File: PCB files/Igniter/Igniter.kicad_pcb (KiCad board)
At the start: 2 copper layers, 124.9 x 69.6 mm, 57 parts, among them IC1 74HC4050, J1 PT, J10 SL2, J11 SL3, J12 SL4, J13 SL5, J14 Micro_SD_Card, J2 PT, J3 PT, J4 PT, J5 Battery +, J6 Battery -, J7 Ignition Coil +, J8 Ignition coil -, J9 SL1, Q1 N MOSFET, Q2 N MOSFET, Q3 N MOSFET, Q4 N MOSFET, Q5 N MOSFET, Q6 N MOSFET, SW1 ARM, U2 FDS8984, U3 FDS8984, U4 FDS8984

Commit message: 12/10/2019
PCB
-Increased 24V trace width to 1 mm
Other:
- net class 24V: trace_width 0.4 -> 1
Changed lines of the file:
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@@
   (net_class 24V ""
     (clearance 0.2)
-    (trace_width 0.4)
+    (trace_width 1)
     (via_dia 0.8)
     (via_drill 0.4)

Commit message: 12/10/2019
-Selected battery molex connector footprint
-Read netlist
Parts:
- removed the J6 at (226.3, 109.0)
- D12: value 3V3 -> 3V3_GOOD
- D13: value 24V -> 24V_ARMED
- J5: value Battery + -> Battery; footprint IgniterCustom:BananaJack15.5mm -> Connector_Molex:Molex_Mini-Fit_Jr_5566-02A_2x01_P4.20mm_Vertical
- moved J5 33.0 mm to (195.6, 105.0), turned to 90 degrees
- moved J10 0.46 mm to (117.1, 143.9)
- moved J11 0.46 mm to (125.4, 143.9)
- moved J12 0.46 mm to (133.6, 143.9)
- moved J8 0.46 mm to (100.7, 143.9)
- moved J9 0.46 mm to (108.9, 143.9)
- renumbered J11 to J10, J12 to J11, J13 to J12, J14 to J13, J7 to J6, J8 to J7, J9 to J8, J10 to J9
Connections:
- J5 pad 2: (no net) -> GNDREF

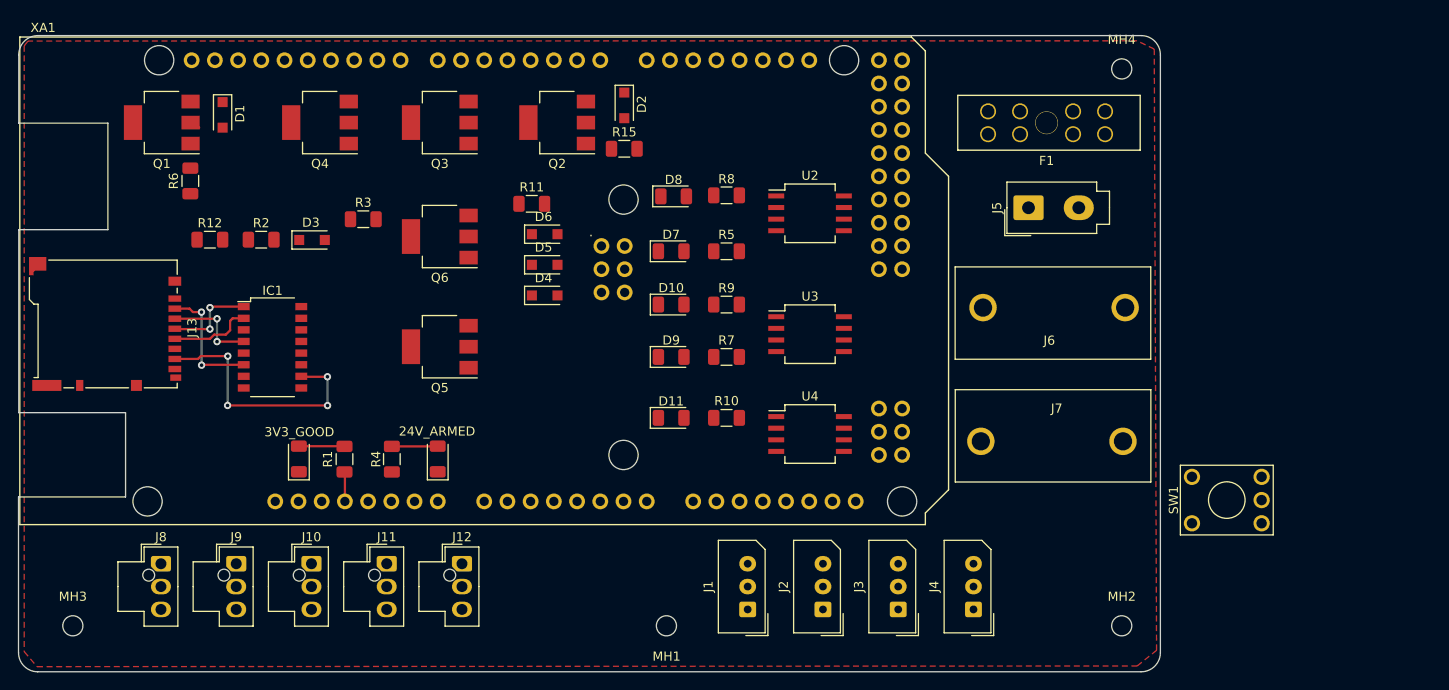
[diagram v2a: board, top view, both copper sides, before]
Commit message: 12/17/2019
-Board layout changes to make better routing paths, no traces drawn yet
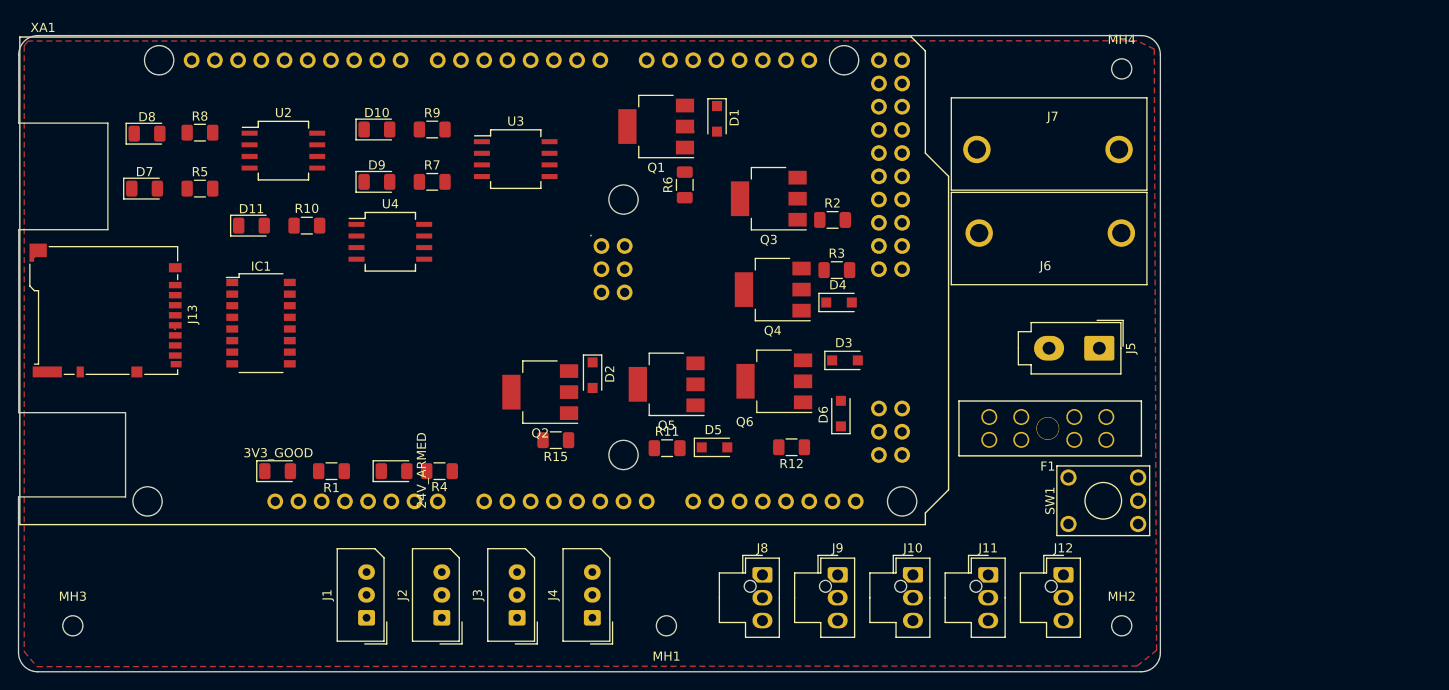
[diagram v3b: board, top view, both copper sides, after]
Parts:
- moved R12 67.6 mm to (169.7, 131.2), turned to 180 degrees
- moved J11 65.8 mm to (191.2, 145.1)
- moved J10 65.8 mm to (182.9, 145.1)
- moved J12 65.8 mm to (199.4, 145.1)
- moved J8 65.8 mm to (166.5, 145.1)
- moved J9 65.8 mm to (174.7, 145.1)
- moved R2 62.5 mm to (174.1, 106.3)
- moved D3 59.8 mm to (175.5, 121.7)
- moved D8 58.0 mm to (99.1, 96.9)
- moved R8 58.0 mm to (104.9, 96.7)
- moved U2 58.0 mm to (114.1, 98.7)
- moved D7 58.0 mm to (98.9, 102.9)
- moved R5 58.0 mm to (104.9, 102.9)
- moved Q1 54.1 mm to (154.9, 96.1)
- moved R6 54.1 mm to (158.0, 102.5)
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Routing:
- net Net-(IC1-Pad10): track 28.3 -> 0.00 mm, vias 4 -> 0
- net Net-(IC1-Pad6): track 13.5 -> 0.00 mm, vias 2 -> 0
- net +3V3: track 13.2 -> 0.11 mm, vias 2 -> 0
- net Net-(IC1-Pad4): track 10.0 -> 0.00 mm, vias 2 -> 0
- net Net-(IC1-Pad2): track 9.07 -> 0.00 mm
- net Net-(D13-Pad2): track 5.02 -> 0.00 mm
- net Net-(D12-Pad2): track 5.00 -> 0.00 mm
- net Net-(D2-Pad2): track 0.69 -> 0.00 mm
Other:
- net class 24V removed
- net class PWR added: clearance 0.2, trace_width 1, via_dia 0.8, via_drill 0.4
- board text added: "Trace direction: FRONT = Vertical BACK = Horizontal"

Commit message: 12/18/2019
-Changed Solenoid connector to SPOX
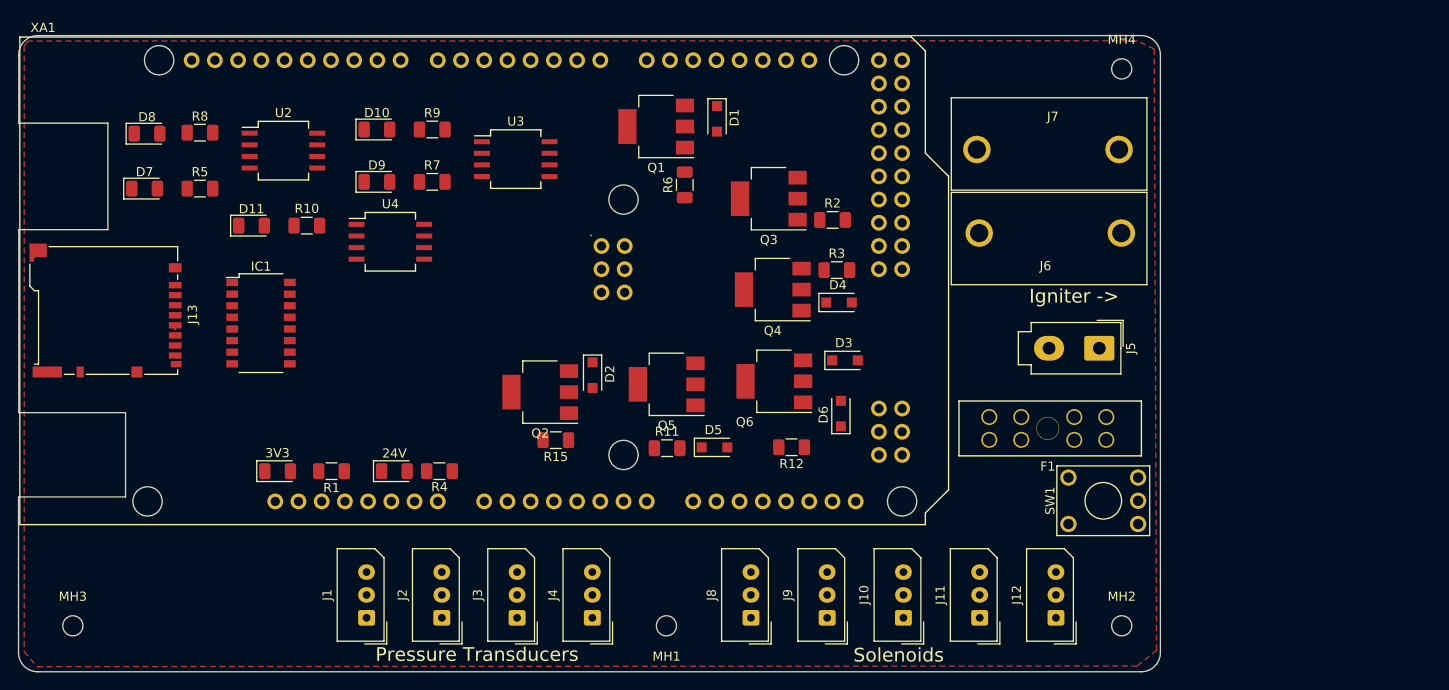
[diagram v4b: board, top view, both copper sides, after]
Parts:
- D12: value 3V3_GOOD -> 3V3
- D13: value 24V_ARMED -> 24V
- J10, J11, J12, J8, J9: footprint Connector_Molex:Molex_Nano-Fit_105309-xx03_1x03_P2.50mm_Vertical -> Connector_Molex:Molex_SPOX_5267-03A_1x03_P2.50mm_Vertical
- moved J8 4.86 mm to (165.2, 149.8), turned to 90 degrees
- moved J9 4.83 mm to (173.6, 149.8), turned to 90 degrees
- moved J10 4.81 mm to (181.9, 149.8), turned to 90 degrees
- moved J11 4.79 mm to (190.2, 149.8), turned to 90 degrees
- moved J12 4.77 mm to (198.6, 149.8), turned to 90 degrees
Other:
- board text added: "Igniter ->"
- board text added: "Pressure Transducers"
- board text added: "Solenoids"

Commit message: 12/21/2019
-Added note to resize board corner mounting holes
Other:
- board text added: "Check diameter"
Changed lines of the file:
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@@
   (general
     (thickness 1.6)
-    (drawings 21)
+    (drawings 26)
     (tracks 4)
     (zones 0)
@@
     )
   )
+  (gr_text "Check diameter" (at 244.53342 150.71598) (layer Dwgs.User)
+    (effects (font (size 1 1) (thickness 0.15)))
+  )
+  (gr_line (start 208.9785 150.71598) (end 237.97768 150.71598) (layer Dwgs.User) (width 0.15))
+  (gr_line (start 208.81594 150.63216) (end 219.95638 157.84068) (layer Dwgs.User) (width 0.15))
+  (gr_line (start 218.8083 145.14576) (end 208.81594 150.63216) (layer Dwgs.User) (width 0.15))
+  (gr_line (start 208.73466 150.79726) (end 218.8083 145.14576) (layer Dwgs.User) (width 0.15))
   (gr_text "Igniter ->" (at 200.56348 114.64544) (layer F.SilkS)
     (effects (font (size 1.5 1.5) (thickness 0.3)))
